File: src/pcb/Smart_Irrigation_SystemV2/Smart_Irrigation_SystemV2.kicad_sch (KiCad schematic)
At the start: 127 parts, among them CN1 PJ-3136-3A, CN2 PJ-3136-3A, CN3 PJ-3136-3A, CN4 PJ-3136-3A, CN5 PJ-3136-3A, CN6 PJ-3136-3A, J1 USB_C_Receptacle_USB2.0_16P, J10 I2C, J11 I2C, J13 I2C, J14 SolarPanel, J15 I2C, J16 GPIO_Expander, J2 FPC_Connector, J6 I2C, J9 Battary Connection, Q1 MUN5211DW1, Q2 FDN340P, Q3 AO3400A, SW1 IO0 Switch, SW2 EN Switch, SW3 SW_Push, SW4 SW_Push, SW5 SW_Push, SW6 SW_Push, U1 CP2102N-Axx-xQFN28, U10 ADS1115IDGS, U11 PCA9536DP, U2 ESP32-WROOM-32, U3 ADS1115IDGS, U4 DS3231MZ, U5 TLV62568ADRL, U6 SN74LVC245APW, U7 TP4056-42-ESOP8, U8 TPS63001, U9 AT24CS32-SSHM

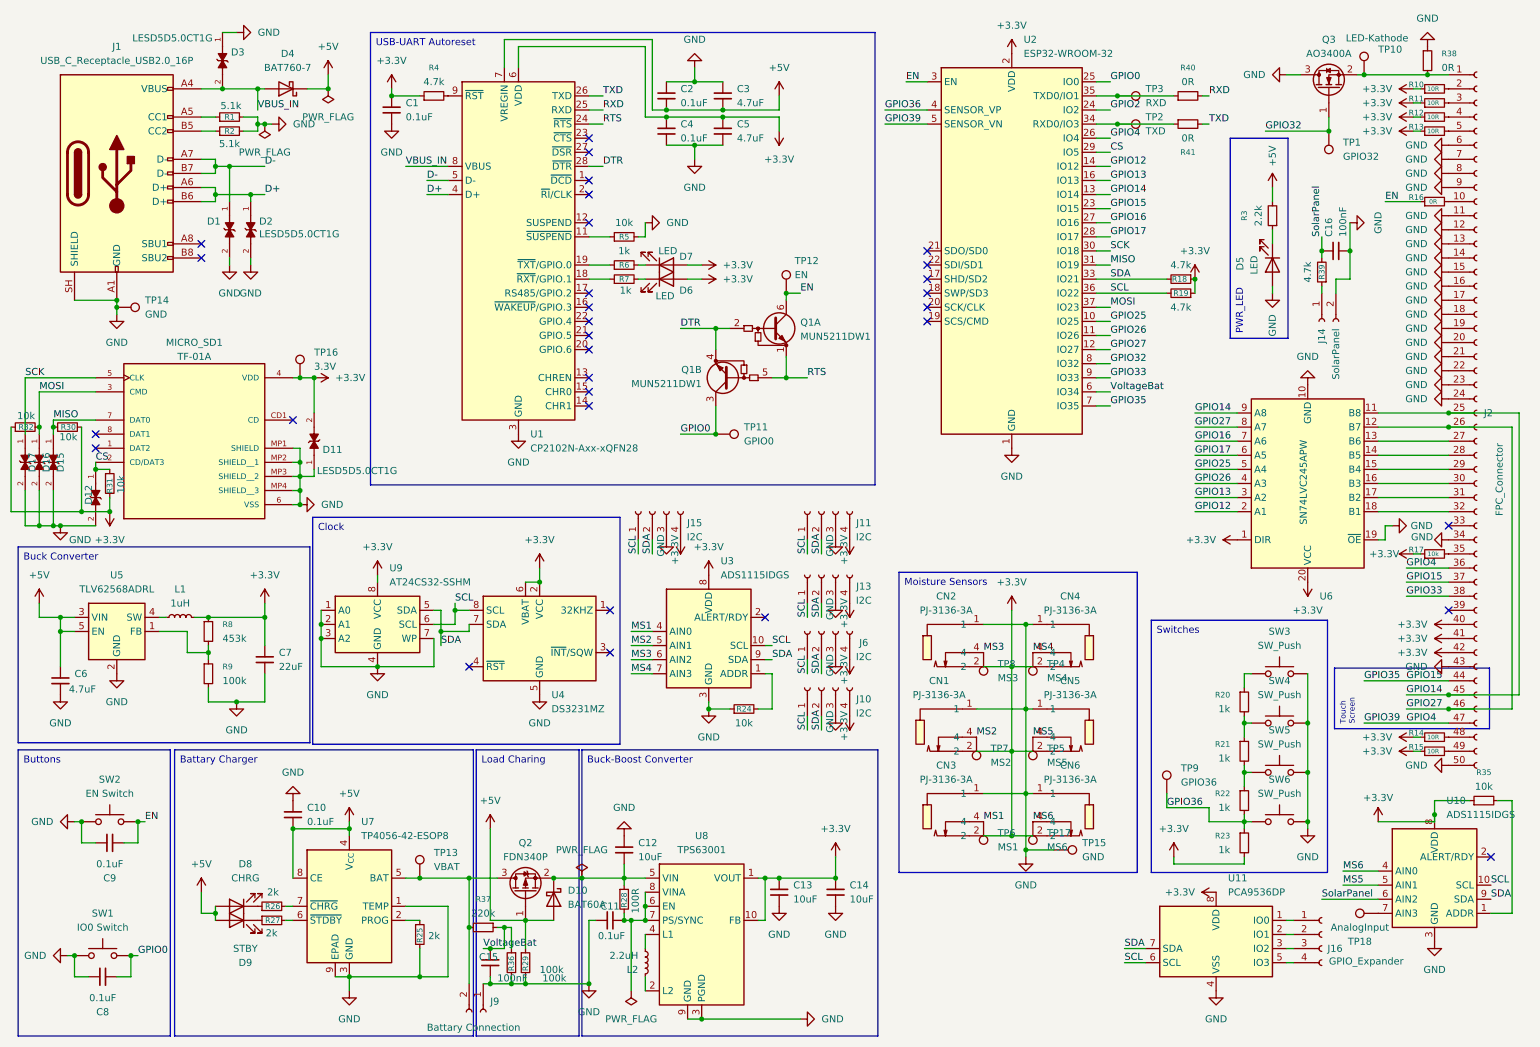
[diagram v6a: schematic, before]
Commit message: added decoupling capacitors
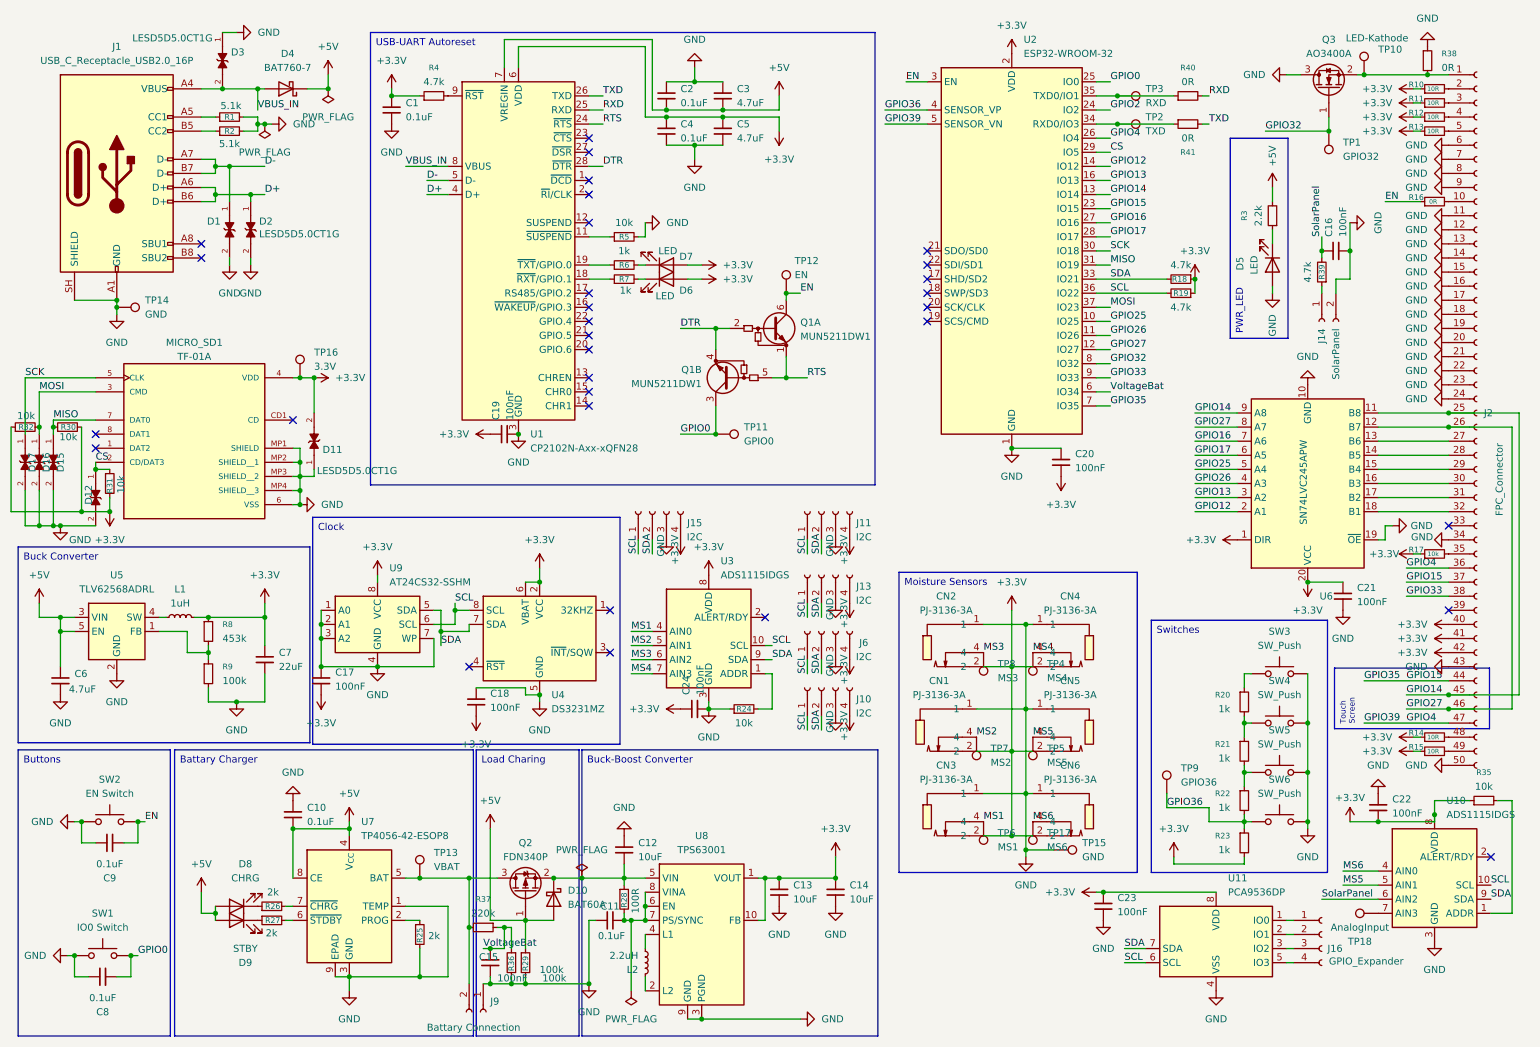
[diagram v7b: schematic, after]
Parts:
- added C17, C18, C19, C20, C21, C22, C23, C24: 100nF, Capacitor_SMD:C_0805_2012Metric, symbol Device:C_Small
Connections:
- net +3.3V: now also C17.2, C18.2, C19.1, C20.2, C21.1, C22.2, C23.1, C24.1
- net GND: now also C17.1, C18.1, C19.2, C20.1, C21.2, C22.1, C23.2, C24.2

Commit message: changed pcb color, fixed design misakes (DRC), made new edge cuts, exported new image of the pcb
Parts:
- removed C19: 100nF, Capacitor_SMD:C_0805_2012Metric, symbol Device:C_Small
- removed TP12: EN, TestPoint:TestPoint_Pad_D1.5mm, symbol Connector:TestPoint
- J1: footprint C5337088:USB-C-SMD_TYPE-C-31-M-12A -> Connector_USB:USB_C_Receptacle_HCTL_HC-TYPE-C-16P-01A
